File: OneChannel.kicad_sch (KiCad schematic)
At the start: 53 parts, among them Q201 NDFPD1N150CG, U201 OPA2156xD, U202 OPA2156xD, U203 OPA2156xD, U204 OPA2156xD

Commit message: V1.3 (improved fine-tuning of CF- and UD-Amps)
PCB Changes:
 - Amplification Poti (1Meg) changed to Offset-Resistor (100k) + Poti (50k) to achieve 20x finer tuning of the amplification

Misc.:
 - Fixed .gitignore to ignore the prl files
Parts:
- added R212, R213: 100k, Resistor_SMD:R_0603_1608Metric, symbol Device:R
- RV201, RV202: value 1M -> 50k
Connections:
- net at C223.2, R204.2, U202.6 (-): now also R212.1; no longer RV201.1, RV201.2
- net at C222.2, R209.2, U204.6 (-): now also R213.1; no longer RV202.1, RV202.2
- new net: R212.2, RV201.1, RV201.2
- new net: R213.2, RV202.1, RV202.2
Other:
- note added: "Offset-R for smaller Poti (finer tuning)"
- note added: "Poti from 30k..50k"
- note added: "R205 & R210: Value needs to be high (100k) to damp track-L which seems to build an LC-Resonance with the feedbackloop of U202B!"
- note removed: "Value needs to be high (100k) to damp track-L which seems to build an LC-Resonance with the feedbackloop of U202B!"
- moved on the sheet: C205, R210, RV201, RV202, TP204, U204B

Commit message: Specified resistor and poti with the values of the buyed ones
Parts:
- R212, R213: value 100k -> 90k9
- RV201, RV202: value 50k -> 47k
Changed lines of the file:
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@@
       (effects (font (size 1.27 1.27)))
     )
-    (property "Value" "100k" (at 215.9 48.508 90)
+    (property "Value" "90k9" (at 215.9 48.508 90)
       (effects (font (size 1.27 1.27)))
     )
@@
       (effects (font (size 1.27 1.27)) (justify right))
     )
-    (property "Value" "50k" (at 225.552 90.678 90)
+    (property "Value" "47k" (at 225.552 90.678 90)
       (effects (font (size 1.27 1.27)) (justify right))
     )
@@
       (effects (font (size 1.27 1.27)))
     )
-    (property "Value" "100k" (at 215.9 88.386 90)
+    (property "Value" "90k9" (at 215.9 88.386 90)
       (effects (font (size 1.27 1.27)))
     )
@@
       (effects (font (size 1.27 1.27)) (justify right))
     )
-    (property "Value" "50k" (at 225.171 50.8 90)
+    (property "Value" "47k" (at 225.171 50.8 90)
       (effects (font (size 1.27 1.27)) (justify right))
     )

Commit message: Removed C202 and adjusted .gitignore
- Added new temporary files to .gitignore
- C202 is not applicable for this circuit and was removed (now an optional part)
- Now using KiCAD 8 (new Project, Board, Schematic files mostly change a bit)
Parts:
- C202: value 100n/25V -> 100n/25V (opt.)

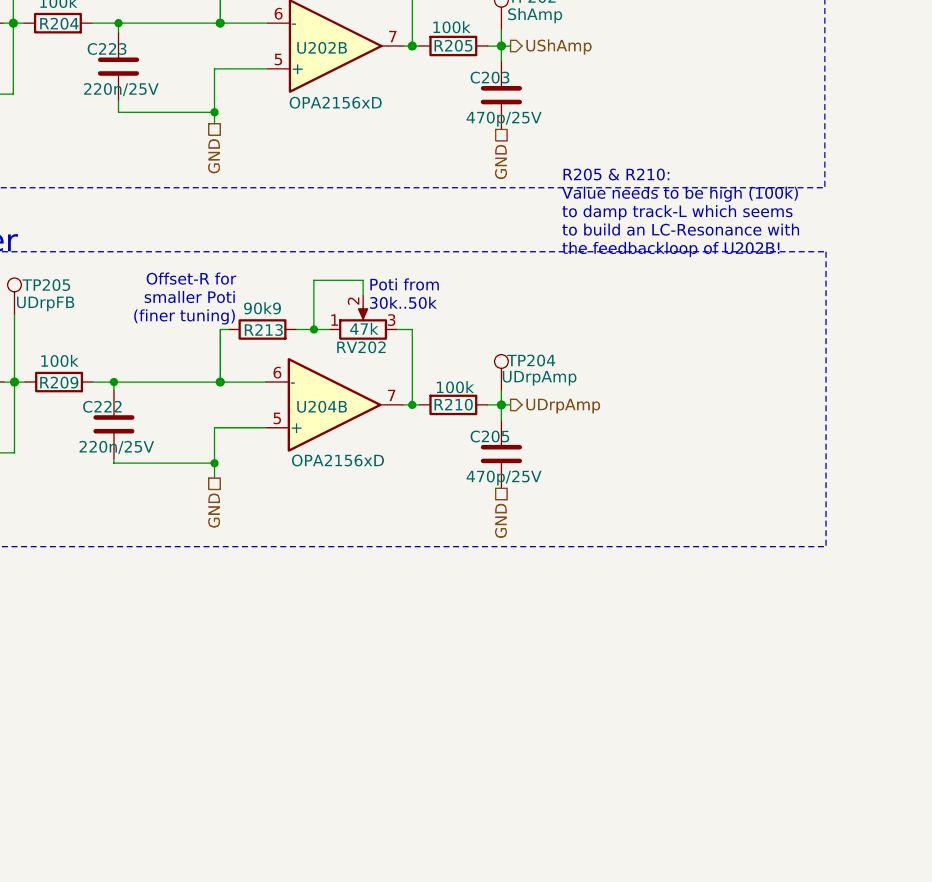
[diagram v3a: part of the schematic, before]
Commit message: Added comments on the UDrp feedback-loop
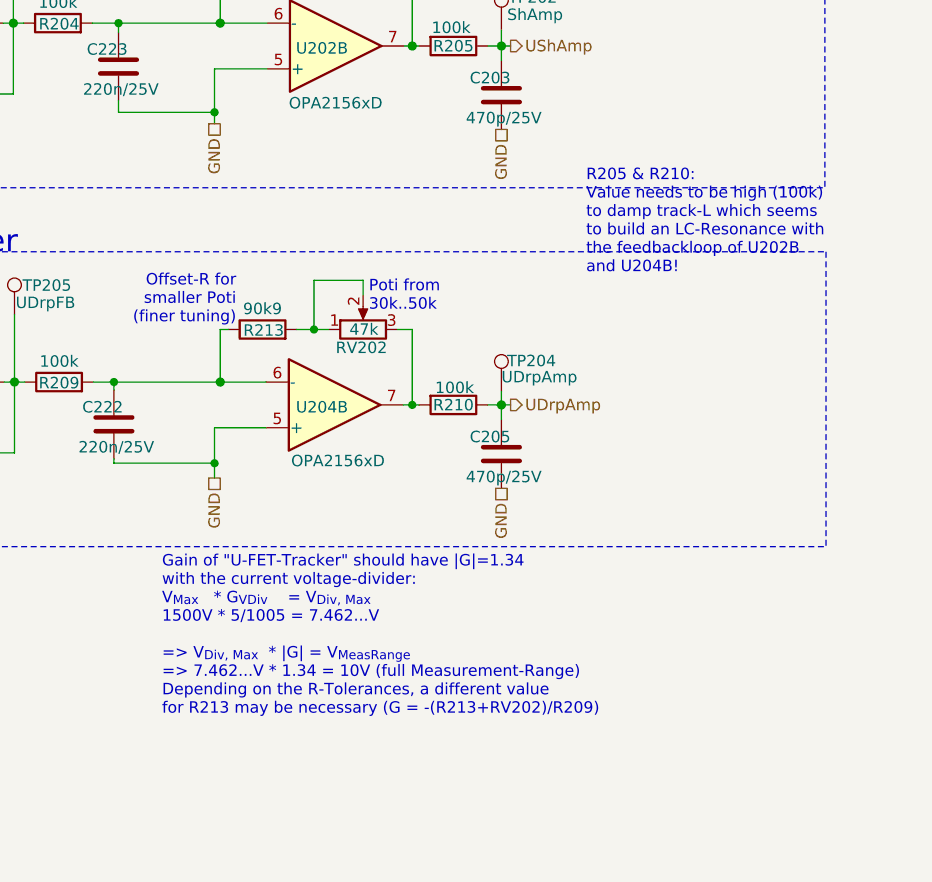
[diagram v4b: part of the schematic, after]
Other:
- note added: "Gain of "U-FET-Tracker" should have |G|=1.34 with the current voltage-divider: V_{Max} * G_{VDiv} = V_{Div, Max} 1500V * 5/1005 = 7.462...V => V_{Div, Max} * |G| = V_{MeasRange} => 7.462...V * 1.34 = 10V (full Measurement-Range) Depending on the R-Tolerances, a different value for R213 may be necessary (G = -(R213+RV202)/R209)"
- note added: "R205 & R210: Value needs to be high (100k) to damp track-L which seems to build an LC-Resonance with the feedbackloop of U202B and U204B!"
- note removed: "R205 & R210: Value needs to be high (100k) to damp track-L which seems to build an LC-Resonance with the feedbackloop of U202B!"
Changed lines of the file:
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@@
+		)
+	)
+	(text "R205 & R210:\nValue needs to be high (100k)\nto damp track-L which seems\nto build an LC-Resonance with\nthe feedbackloop of U202B\nand U204B!"
+		(exclude_from_sim no)
+		(at 251.86 84.6 0)
+		(effects
+			(font
+				(size 1.27 1.27)
+			)
+			(justify left bottom)
 		)
 	)
@@
 		)
 	)
-	(text "R205 & R210:\nValue needs to be high (100k)\nto damp track-L which seems\nto build an LC-Resonance with\nthe feedbackloop of U202B!"
+	(text "Gain of \"U-FET-Tracker\" should have |G|=1.34\nwith the current voltage-divider:\nV_{Max}   * G_{VDiv}    = V_{Div, Max}\n1500V * 5/1005 = 7.462...V\n\n=> V_{Div, Max}  * |G| = V_{MeasRange}\n=> 7.462...V * 1.34 = 10V (full Measurement-Range)\nDepending on the R-Tolerances, a different value\nfor R213 may be necessary (G = -(R213+RV202)/R209)"
 		(exclude_from_sim no)
-		(at 249.174 82.677 0)
+		(at 204.73 124.74 0)
 		(effects
 			(font
 				(size 1.27 1.27)
 			)
-			(justify left bottom)
+			(justify left)
 		)
 	)
